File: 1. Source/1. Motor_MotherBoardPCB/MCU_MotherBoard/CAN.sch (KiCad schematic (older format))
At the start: 2 parts, among them J8 Connector_JST_01x03, U19 CAN_TJA1051

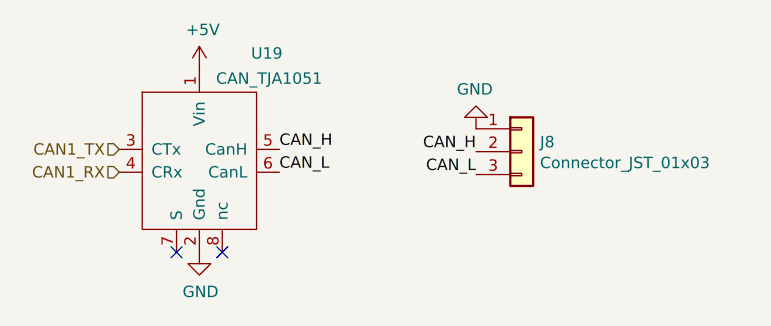
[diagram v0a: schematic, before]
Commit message: Schematic finished
- change cap`s footprint to smd type
- artwork should be done.
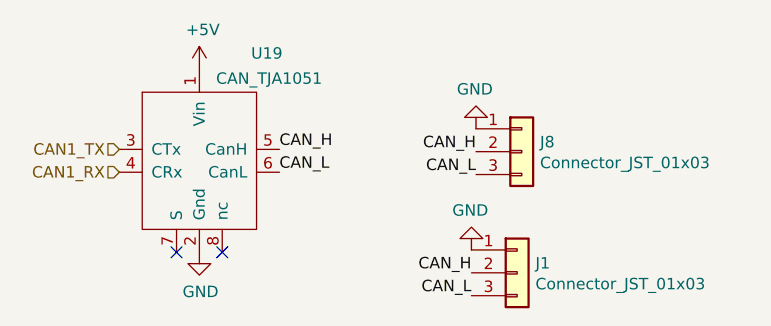
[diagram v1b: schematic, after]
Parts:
- added J1: Connector_JST_01x03, Connectors_JST:JST_XH_S03B-XH-A_03x2.50mm_Angled, symbol BC_Connectors:Connector_JST_01x03
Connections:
- net CAN_H: now also J1.2 (Pin_2)
- net CAN_L: now also J1.3 (Pin_3)
- net GND: now also J1.1 (Pin_1)
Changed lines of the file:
@@
+	-1   0    0    1
+$EndComp
+$Comp
+L BC_Connectors:Connector_JST_01x03 J?
+U 1 1 638BC967
+P 5445 2870
+AR Path="/6387462E/638BC967" Ref="J?"  Part="1"
+AR Path="/6386E3EE/638BC967" Ref="J1"  Part="1"
+F 0 "J1" H 5525 2912 50  0000 L CNN
+F 1 "Connector_JST_01x03" H 5525 2821 50  0000 L CNN
+F 2 "Connectors_JST:JST_XH_S03B-XH-A_03x2.50mm_Angled" H 5445 2870 50  0001 C CNN
+F 3 "" H 5445 2870 50  0001 C CNN
+	1    5445 2870
+	1    0    0    -1
+$EndComp
+Text Label 5245 2970 2    50   ~ 0
+CAN_L
+Text Label 5245 2870 2    50   ~ 0
+CAN_H
+$Comp
+L power:GND #PWR?
+U 1 1 638BC96F
+P 5245 2770
+AR Path="/6387462E/638BC96F" Ref="#PWR?"  Part="1"
+AR Path="/6386E3EE/638BC96F" Ref="#PWR024"  Part="1"
+F 0 "#PWR024" H 5245 2520 50  0001 C CNN
+F 1 "GND" H 5250 2597 50  0000 C CNN
+F 2 "" H 5245 2770 50  0001 C CNN
+F 3 "" H 5245 2770 50  0001 C CNN
+	1    5245 2770
 	-1   0    0    1
 $EndComp
